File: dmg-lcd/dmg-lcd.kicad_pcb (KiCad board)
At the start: 2 copper layers, 81 x 79 mm, 25 parts, among them J1 Conn_01x01_Pin, J10 Conn_01x01, J2 Conn_01x01_Pin, J3 LCD Connector, J4 LCD Dev Header, J5 Conn_01x02, J6 Conn_01x05, J7 Conn_01x05, J8 Conn_01x02, J9 Conn_01x02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

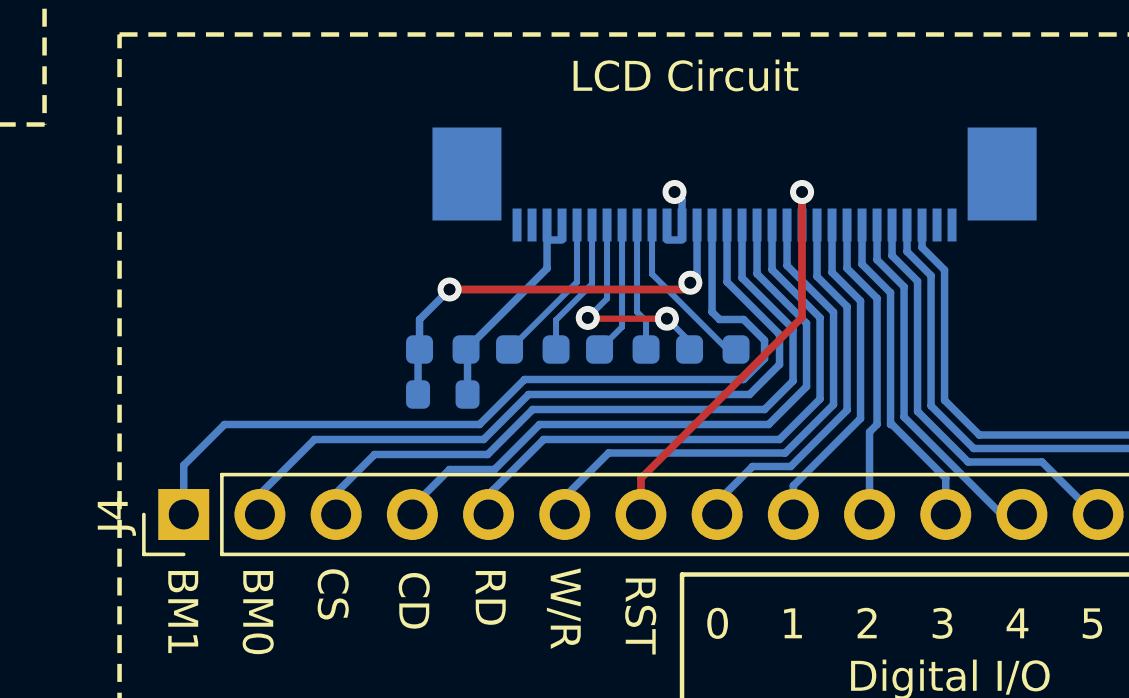
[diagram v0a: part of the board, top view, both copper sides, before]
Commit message: feat: Update one of the capacitor footprints to match what is in stock, rerouting too
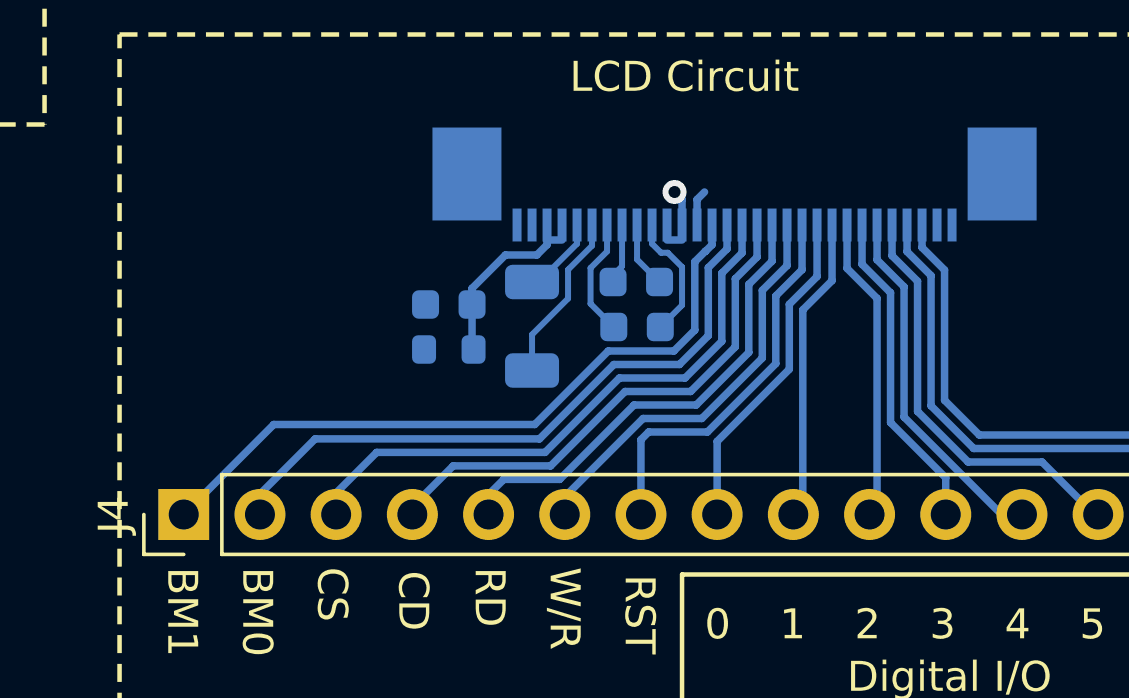
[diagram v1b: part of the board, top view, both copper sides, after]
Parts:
- C2: footprint Capacitor_SMD:C_0603_1608Metric -> Capacitor_SMD:C_1206_3216Metric
- moved C3 2.63 mm to (137.2, 69.2)
- moved C4 2.29 mm to (137.2, 67.8)
- moved C1 1.51 mm to (131.0, 68.5)
- moved R1 1.51 mm to (131.0, 70.0)
- moved C2 0.78 mm to (133.8, 69.2), turned to -90 degrees
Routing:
- net VSS: track 13.6 -> 1.27 mm, vias 2 -> 0
- net BM1: track 27.6 -> 22.8 mm
- net RD(E): track 18.3 -> 14.7 mm
- net WR: track 16.4 -> 12.8 mm
- net CS0: track 22.2 -> 18.6 mm
- net CD: track 20.4 -> 16.8 mm
- net BM0: track 24.0 -> 20.6 mm
- net VB0-: track 6.85 -> 3.95 mm, vias 2 -> 0
- net VS+: track 4.58 -> 2.65 mm
- net VB1-: track 3.96 -> 2.12 mm
- net VB1+: track 3.77 -> 2.21 mm
- net RST: track 14.6 -> 13.0 mm, vias 1 -> 0
- net VS-: track 4.15 -> 5.68 mm
- net D0: track 11.7 -> 10.5 mm
- net D1: track 10.5 -> 9.68 mm
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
